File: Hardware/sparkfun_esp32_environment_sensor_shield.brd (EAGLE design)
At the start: 58.4 x 50.8 mm, 52 parts, among them J1 WEATHER_METER-WIND, J2 WEATHER_METER-RAIN, U1 BME280, U2 CCS811, U3 TSL2561FN

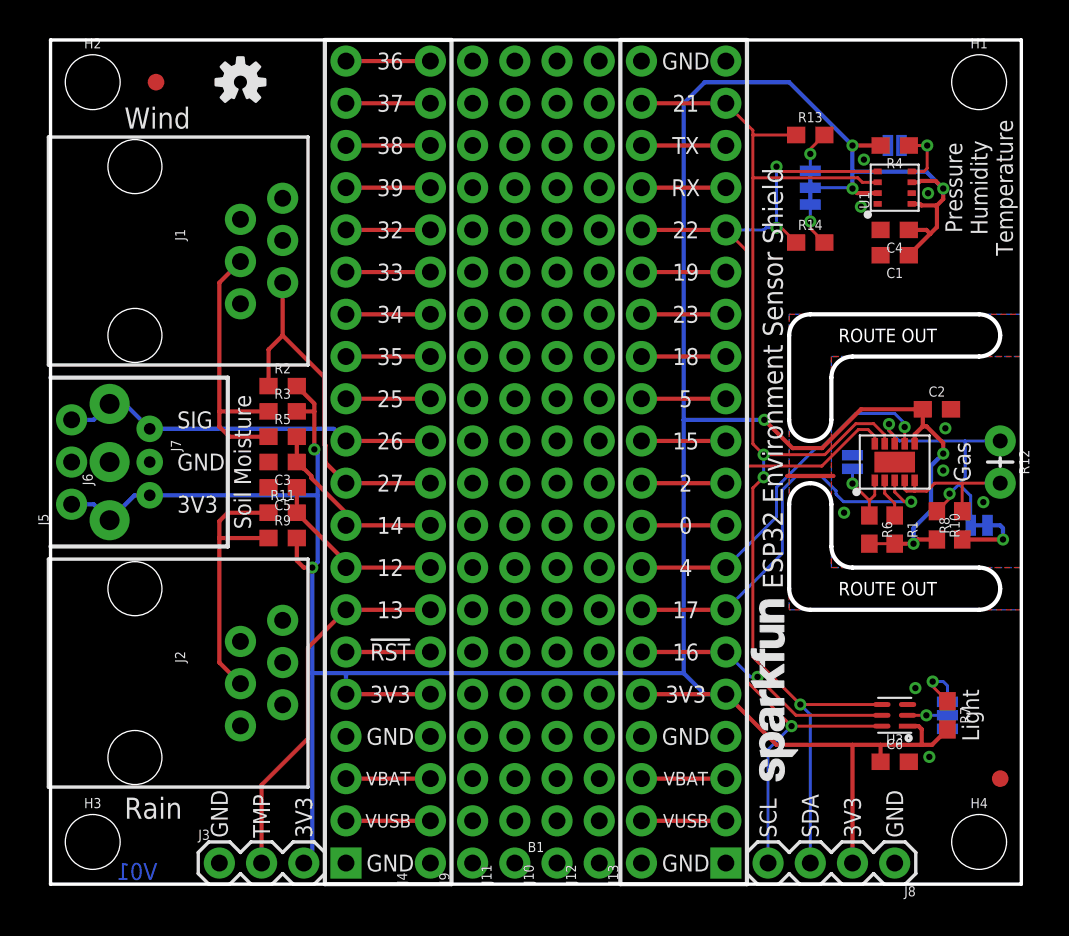
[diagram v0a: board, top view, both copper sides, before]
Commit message: Schematic cleanup. Bussing inner prototyping pins together.
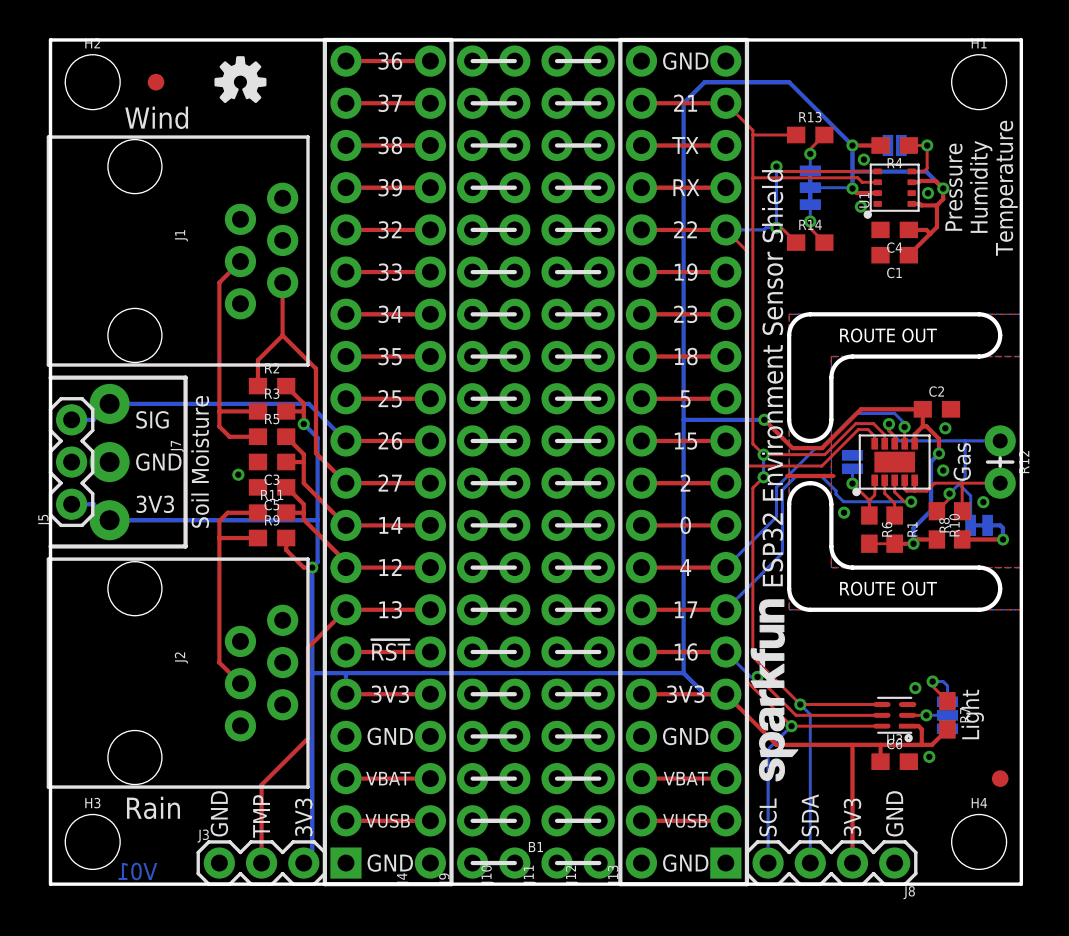
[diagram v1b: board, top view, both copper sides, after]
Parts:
- removed J6: (no value), SparkFun-Connectors:JST-3-PTH-NS
- J5: device SparkFun-Connectors:1X03_NO_SILK -> SparkFun-Connectors:1X03
- R12: value 10k -> DNP
- moved J10 2.54 mm to (27.9, 1.27)
- moved J11 2.54 mm to (30.5, 1.27)
- moved C3 0.63 mm to (13.3, 25.4)
- moved C5 0.63 mm to (13.3, 23.9)
- moved R11 0.63 mm to (13.3, 22.4)
- moved R2 0.63 mm to (13.3, 30.0)
- moved R3 0.63 mm to (13.3, 28.4)
- moved R5 0.63 mm to (13.3, 26.9)
- moved R9 0.63 mm to (13.3, 20.8)
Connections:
- new net N$29: J11.1, J12.1
- new net N$30: J11.2, J12.2
- new net N$31: J11.3, J12.3
- new net N$32: J11.4, J12.4
- new net N$33: J11.5, J12.5
- new net N$34: J11.6, J12.6
- new net N$35: J11.7, J12.7
- new net N$36: J11.8, J12.8
- new net N$37: J11.9, J12.9
- new net N$38: J11.10, J12.10
- new net N$39: J11.11, J12.11
- new net N$40: J11.12, J12.12
- new net N$41: J11.13, J12.13
- new net N$42: J11.14, J12.14
- new net N$43: J11.15, J12.15
- new net N$44: J11.16, J12.16
- new net N$45: J11.17, J12.17
- new net N$46: J11.18, J12.18
- new net N$47: J11.19, J12.19
- new net N$48: J11.20, J12.20
- new net N$49: J10.1, J9.1
- new net N$50: J10.2, J9.2
- new net N$51: J10.3, J9.3
- new net N$52: J10.4, J9.4
- new net N$53: J10.5, J9.5
- new net N$54: J10.6, J9.6
- new net N$55: J10.7, J9.7
- new net N$56: J10.8, J9.8
- new net N$57: J10.9, J9.9
- new net N$58: J10.10, J9.10
- new net N$59: J10.11, J9.11
- new net N$60: J10.12, J9.12
- new net N$61: J10.13, J9.13
- new net N$62: J10.14, J9.14
- new net N$63: J10.15, J9.15
- new net N$64: J10.16, J9.16
- new net N$65: J10.17, J9.17
- new net N$66: J10.18, J9.18
- new net N$67: J10.19, J9.19
- new net N$68: J10.20, J9.20
- net 3.3V: no longer J6.1
- net GND: no longer J6.2
- net SOIL_MOISTURE: no longer J6.3
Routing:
- net N$68: track 0.00 -> 2.54 mm
- net N$67: track 0.00 -> 2.54 mm
- net N$66: track 0.00 -> 2.54 mm
- net N$65: track 0.00 -> 2.54 mm
- net N$64: track 0.00 -> 2.54 mm
- net N$63: track 0.00 -> 2.54 mm
- net N$62: track 0.00 -> 2.54 mm
- net N$61: track 0.00 -> 2.54 mm
- net N$60: track 0.00 -> 2.54 mm
- net N$59: track 0.00 -> 2.54 mm
- net N$58: track 0.00 -> 2.54 mm
- net N$57: track 0.00 -> 2.54 mm
- net N$56: track 0.00 -> 2.54 mm
- net N$55: track 0.00 -> 2.54 mm
- net N$54: track 0.00 -> 2.54 mm
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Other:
- board text added: "10kΩ NTC"
- board text added: "External Temperature"
- board text added: "I C Extension"

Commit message: Connecting CCS811 RST pin to ESP32.
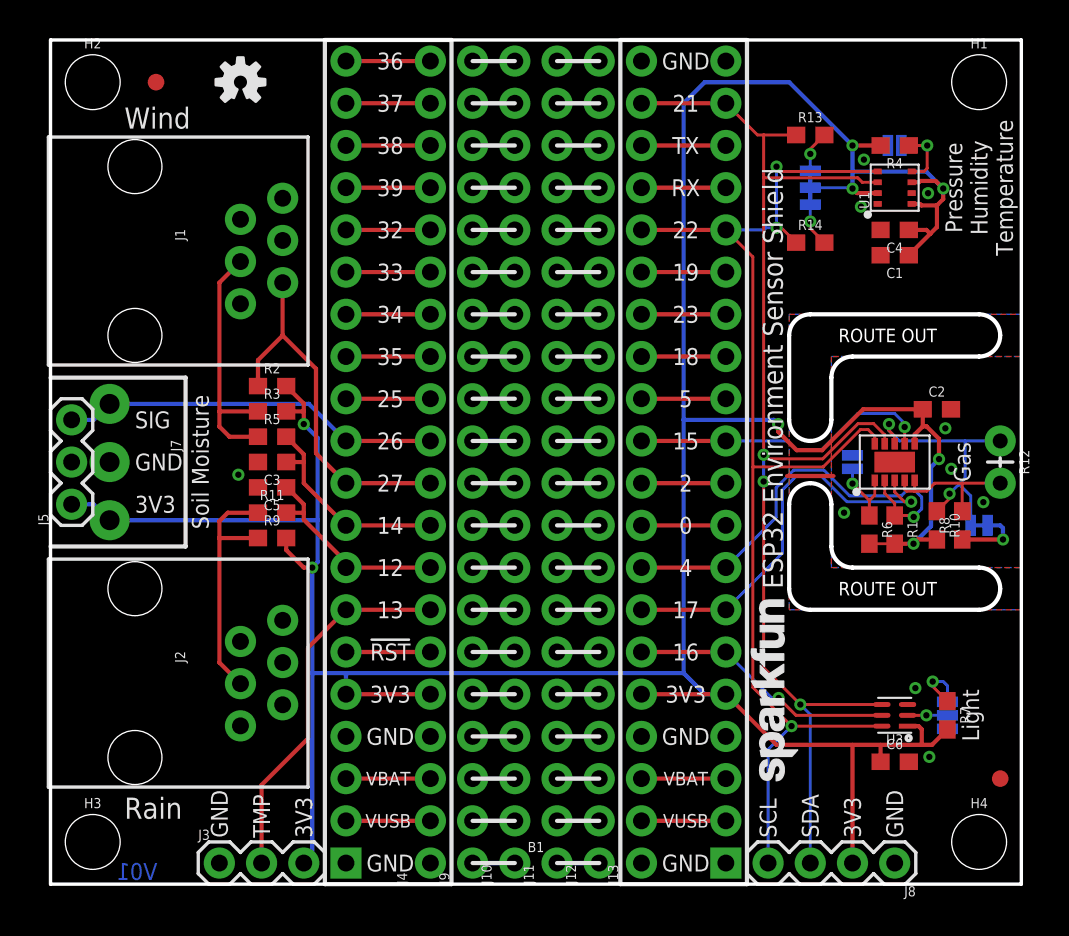
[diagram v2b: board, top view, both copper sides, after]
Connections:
- removed net N$22: B1.30, J13.11
- net CCS811_!RST!: now also B1.33, J13.8
- net CCS811_!WAKE!: now also B1.30, J13.11; no longer B1.33, J13.8
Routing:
- net CCS811_!RST!: track 2.36 -> 26.2 mm, vias 0 -> 1
- net N$22: track 5.08 -> 0.00 mm
- net CCS811_!WAKE!: track 22.2 -> 18.4 mm
- net SDA: track 77.5 -> 76.0 mm

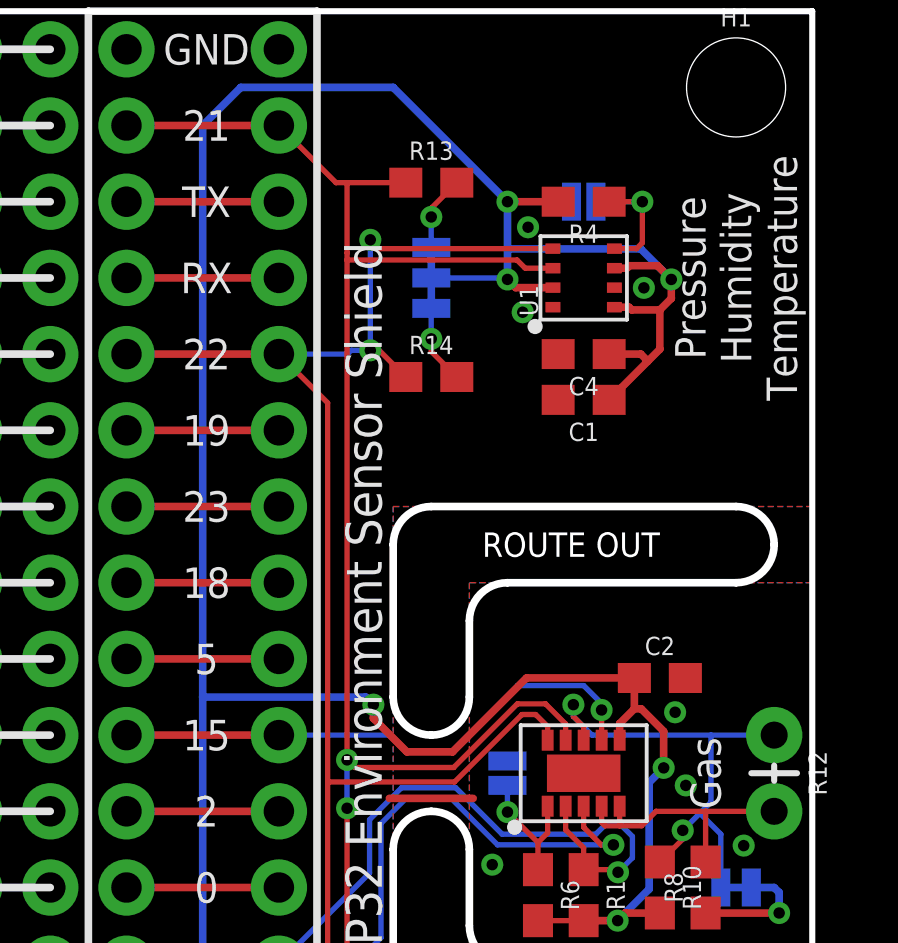
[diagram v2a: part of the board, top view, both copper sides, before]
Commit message: Labeling in-use pins on bottom side.
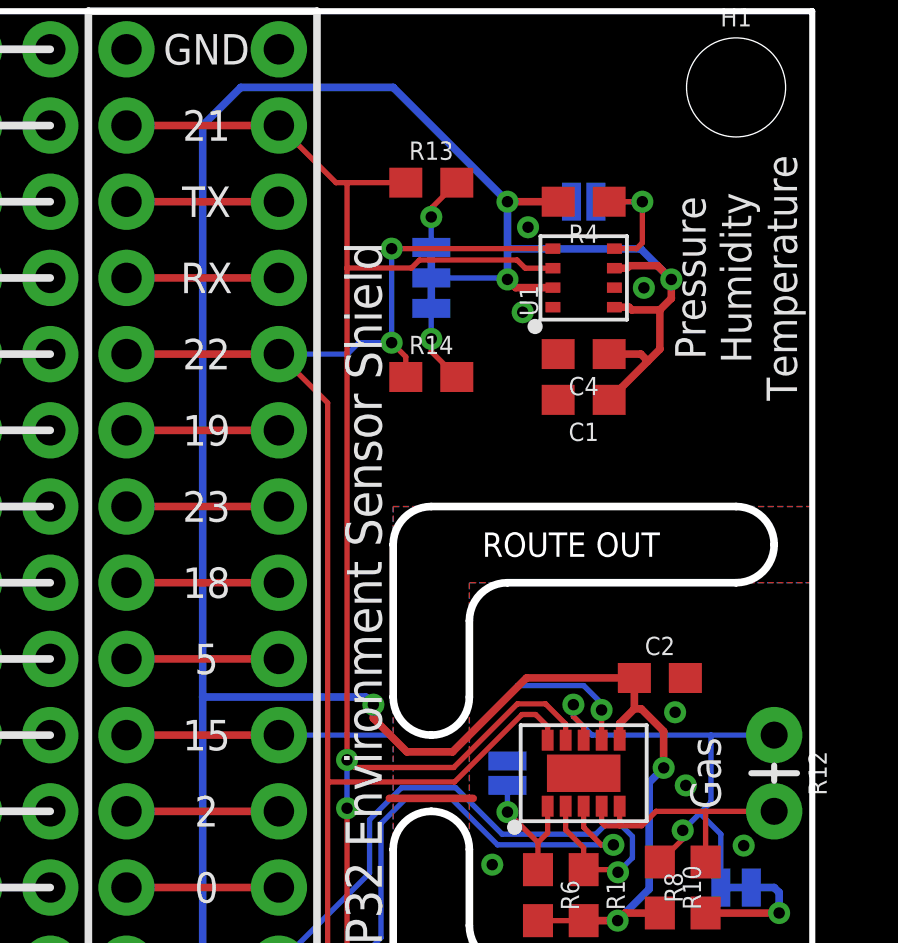
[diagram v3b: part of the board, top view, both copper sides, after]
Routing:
- net SCL: track 74.3 -> 73.5 mm
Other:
- board text added: "GAS !INT!"
- board text added: "GAS !RST!"
- board text added: "GAS !WAKE!"
- board text added: "LUX-INT"
- board text added: "RAIN"
- board text added: "SOIL"
- board text added: "WIND DIR"
- board text added: "WIND SPEED"
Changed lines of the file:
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@@
 <text x="55.88" y="25.4" size="0.889" layer="22" ratio="15" rot="MR270" align="bottom-center">10kΩ
 NTC</text>
+<text x="41.783" y="16.51" size="0.889" layer="22" font="vector" ratio="15" rot="MR0" align="center-right">GAS
+!INT!</text>
+<text x="41.656" y="13.97" size="0.889" layer="22" font="vector" ratio="15" rot="MR0" align="center-right">LUX-INT</text>
+<text x="41.783" y="19.05" size="0.889" layer="22" font="vector" ratio="15" rot="MR0" align="center-right">GAS
+!RST!</text>
+<text x="41.783" y="26.67" size="0.889" layer="22" font="vector" ratio="15" rot="MR0" align="center-right">GAS
+!WAKE!</text>
+<text x="41.783" y="39.37" size="0.889" layer="22" font="vector" ratio="15" rot="MR0" align="center-right">SCL</text>
+<text x="41.783" y="46.99" size="0.889" layer="22" font="vector" ratio="15" rot="MR0" align="center-right">SDA</text>
+<text x="16.891" y="17.272" size="0.889" layer="22" font="vector" ratio="15" rot="MR0" align="center-left">TMP</text>
+<text x="16.51" y="19.05" size="0.889" layer="22" font="vector" ratio="15" rot="MR0" align="center-left">RAIN</text>
+<text x="16.51" y="21.59" size="0.889" layer="22" font="vector" ratio="15" rot="MR0" align="center-left">WIND
+SPEED</text>
+<text x="16.51" y="24.13" size="0.889" layer="22" font="vector" ratio="15" rot="MR0" align="center-left">WIND
+DIR</text>
+<text x="16.51" y="26.67" size="0.889" layer="22" font="vector" ratio="15" rot="MR0" align="center-left">SOIL</text>
 </plain>
 <attributes>
@@
 <wire x1="44.592" y1="9.51" x2="43.18" y2="8.098" width="0.1778" layer="16"/>
 <wire x1="43.18" y1="8.098" x2="43.18" y2="1.27" width="0.1778" layer="16"/>
-<via x="43.688" y="39.497" extent="1-16" drill="0.381"/>
-<wire x1="43.688" y1="39.497" x2="43.688" y2="43.18" width="0.1778" layer="16"/>
-<via x="43.688" y="43.18" extent="1-16" drill="0.381"/>
-<wire x1="43.688" y1="43.18" x2="43.983" y2="42.885" width="0.1778" layer="1"/>
-<wire x1="43.983" y1="42.885" x2="49.775" y2="42.885" width="0.1778" layer="1"/>
+<via x="44.3992" y="39.751" extent="1-16" drill="0.381"/>
 <wire x1="46.4947" y1="25.1079" x2="48.7426" y2="27.3558" width="0.1778" layer="1"/>
 <contactref element="J13" pad="16"/>
 <wire x1="35.56" y1="39.37" x2="40.64" y2="39.37" width="0.254" layer="1"/>
 <wire x1="42.926" y1="39.37" x2="40.64" y2="39.37" width="0.1778" layer="16"/>
-<wire x1="44.87" y1="38.608" x2="43.981" y2="39.497" width="0.1778" layer="1"/>
-<wire x1="43.981" y1="39.497" x2="43.688" y2="39.497" width="0.1778" layer="1"/>
-<wire x1="42.926" y1="39.37" x2="43.053" y2="39.497" width="0.1778" layer="16"/>
-<wire x1="43.053" y1="39.497" x2="43.688" y2="39.497" width="0.1778" layer="16"/>
 <wire x1="46.4947" y1="25.1079" x2="42.2656" y2="25.1079" width="0.1778" layer="1"/>
 <wire x1="44.592" y1="9.51" x2="42.2656" y2="11.8364" width="0.1778" layer="1"/>
@@
 <wire x1="42.2656" y1="25.1079" x2="42.2656" y2="37.7444" width="0.1778" layer="1"/>
 <wire x1="42.2656" y1="37.7444" x2="40.64" y2="39.37" width="0.1778" layer="1"/>
+<wire x1="42.926" y1="39.37" x2="43.307" y2="39.751" width="0.1778" layer="16"/>
+<wire x1="43.307" y1="39.751" x2="44.3992" y2="39.751" width="0.1778" layer="16"/>
+<wire x1="44.3992" y1="39.751" x2="44.3992" y2="42.885" width="0.1778" layer="16"/>
+<via x="44.3992" y="42.885" extent="1-16" drill="0.381"/>
+<wire x1="44.3992" y1="42.885" x2="49.775" y2="42.885" width="0.1778" layer="1"/>
+<wire x1="44.87" y1="38.608" x2="44.87" y2="39.2802" width="0.1778" layer="1"/>
+<wire x1="44.87" y1="39.2802" x2="44.3992" y2="39.751" width="0.1778" layer="1"/>
 </signal>
 <signal name="SDA">
@@
 <wire x1="43.1673" y1="25.5905" x2="42.9133" y2="25.8445" width="0.1778" layer="1"/>
 <wire x1="42.9133" y1="13.0175" x2="42.9133" y2="24.2316" width="0.1778" layer="1"/>
-<wire x1="42.9133" y1="25.8445" x2="42.9133" y2="42.5069" width="0.1778" layer="1"/>
-<wire x1="42.9133" y1="42.7482" x2="42.9133" y2="45.085" width="0.1778" layer="1"/>
+<wire x1="42.9133" y1="25.8445" x2="42.9133" y2="42.2148" width="0.1778" layer="1"/>
+<wire x1="42.9133" y1="42.2402" x2="42.9133" y2="45.085" width="0.1778" layer="1"/>
 <wire x1="42.9133" y1="45.085" x2="42.545" y2="45.085" width="0.1778" layer="1"/>
-<wire x1="48.5775" y1="42.5069" x2="42.9133" y2="42.5069" width="0.1778" layer="1"/>
-<wire x1="42.9133" y1="42.5069" x2="42.9133" y2="42.7482" width="0.1778" layer="1"/>
+<wire x1="48.5775" y1="42.5069" x2="45.3263" y2="42.5069" width="0.1778" layer="1"/>
+<wire x1="45.3263" y1="42.5069" x2="45.0596" y2="42.2402" width="0.1778" layer="1"/>
+<wire x1="45.0596" y1="42.2402" x2="42.9133" y2="42.2402" width="0.1778" layer="1"/>
+<wire x1="42.9133" y1="42.2402" x2="42.9133" y2="42.2148" width="0.1778" layer="1"/>
 </signal>
 <signal name="3.3V">
